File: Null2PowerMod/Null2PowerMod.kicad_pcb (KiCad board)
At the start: 2 copper layers, 18 x 28 mm, 35 parts, among them CN4 USB_C_Receptacle_USB2.0, J1 Conn_01x01, J2 Conn_01x08, J3 Conn_01x01, J4 Conn_01x01, J5 Conn_01x01, T1 MMUN2133LT1G, U1 TPS61030PWP, U2 MCP73871

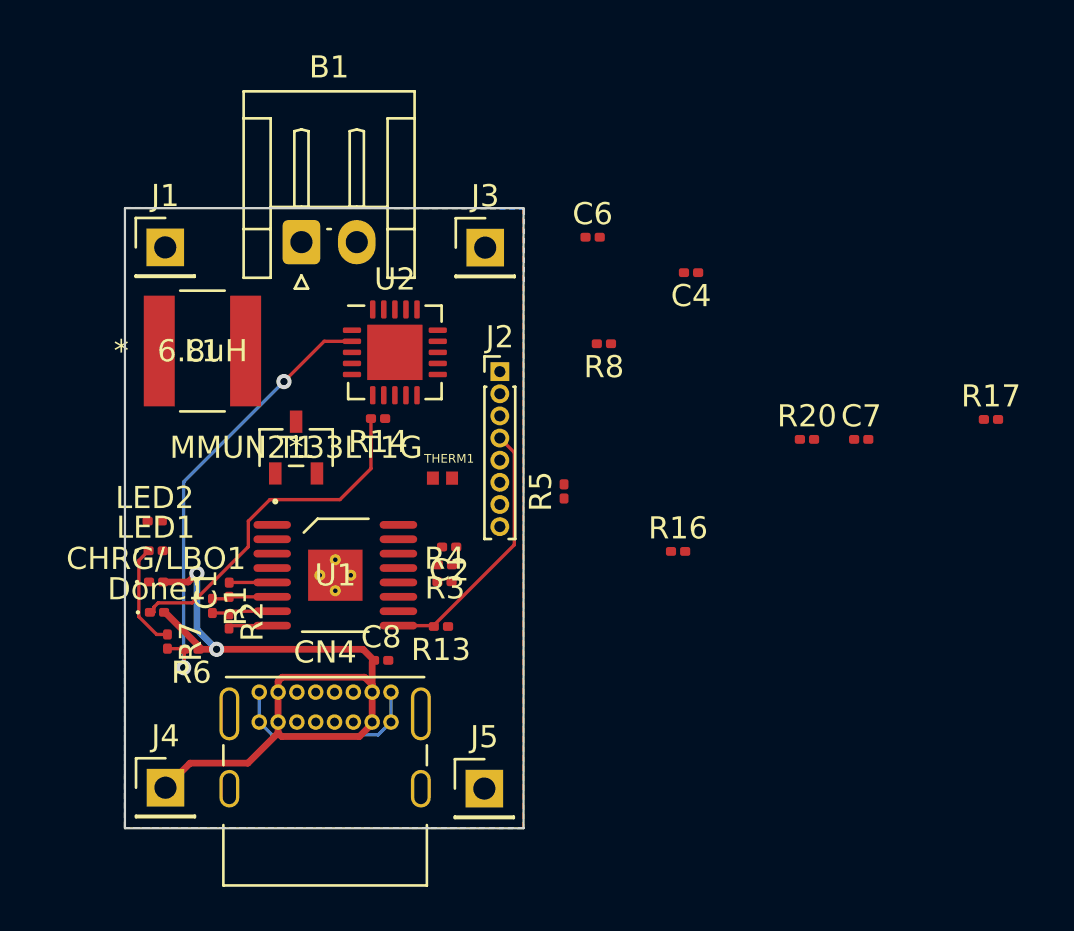
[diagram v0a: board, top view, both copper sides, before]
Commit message: Trying out an autorouter
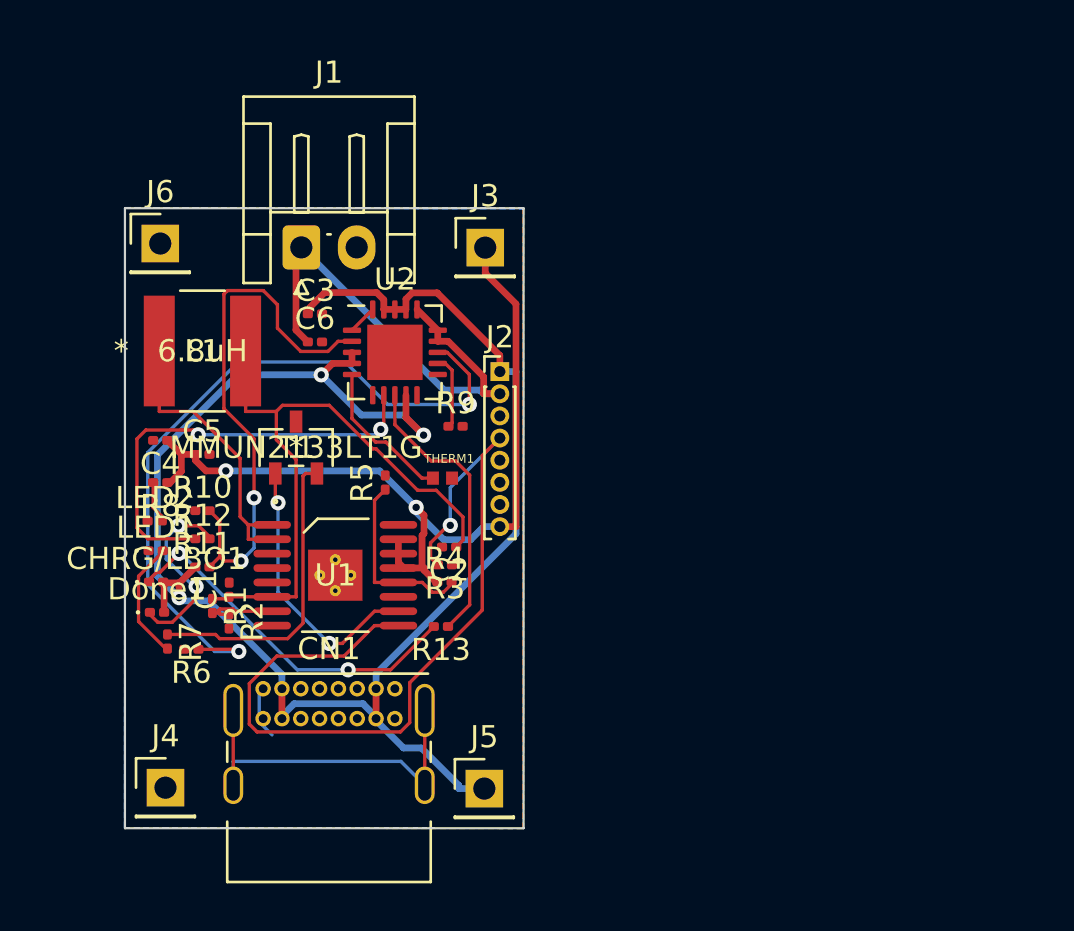
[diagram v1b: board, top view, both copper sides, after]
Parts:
- removed B1: Conn_01x02_Female, Connector_JST:JST_EH_S2B-EH_1x02_P2.50mm_Horizontal
- removed C7, C8: 10μF, Capacitor_SMD:C_0201_0603Metric
- removed CN4: USB_C_Receptacle_USB2.0, Connector_USB:USB_C_Receptacle_GCT_USB4085
- removed R14, R16, R20: 1k, Resistor_SMD:R_0201_0603Metric
- removed R17: 100k, Resistor_SMD:R_0201_0603Metric
- added C3: 10μF, Capacitor_SMD:C_0201_0603Metric, F.Cu at (68.6, 64.8)
- added C5: 100μF, Capacitor_SMD:C_0201_0603Metric, F.Cu at (63.5, 71.1)
- added CN1: USB_C_Receptacle_USB2.0, Connector_USB:USB_C_Receptacle_GCT_USB4085, F.Cu at (66.2, 81.7)
- added J6: Conn_01x01, Connector_PinHeader_2.54mm:PinHeader_1x01_P2.54mm_Vertical, F.Cu at (61.6, 61.6)
- added R10: 100k, Resistor_SMD:R_0201_0603Metric, F.Cu at (63.5, 73.7)
- added R11: 270k, Resistor_SMD:R_0201_0603Metric, F.Cu at (63.5, 76.2)
- added R12: 1k, Resistor_SMD:R_0201_0603Metric, F.Cu at (63.5, 74.9)
- added R9: 100k, Resistor_SMD:R_0201_0603Metric, F.Cu at (74.9, 69.8)
- C2: value 2.2μF -> 0.1μF
- C4: value 0.1μF -> 2.2μF
- C6: value 100μF -> 10μF
- J1: value Conn_01x01 -> Conn_01x02; footprint Connector_PinHeader_2.54mm:PinHeader_1x01_P2.54mm_Vertical -> Connector_JST:JST_EH_S2B-EH_1x02_P2.50mm_Horizontal
- R13: value 200k -> 1k
- R3: value 1.87M -> 200k
- R4: value 200k -> 1.87M
- R5: value 1k -> 200k; footprint Capacitor_SMD:C_0201_0603Metric -> Resistor_SMD:R_0201_0603Metric
- R6: value 270k -> 1k
- R7: value 100k -> 1k
- R8: footprint Resistor_SMD:R_0201_0603Metric -> Capacitor_SMD:C_0201_0603Metric
- moved C4 25.1 mm to (61.6, 70.5)
- moved R8 21.0 mm to (61.6, 72.4)
- moved C6 13.4 mm to (68.6, 66.0)
- moved R5 8.08 mm to (71.8, 72.4)
- moved J1 6.15 mm to (68.0, 61.8)
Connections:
- C2 pad 1: +5V -> Net-(C1-Pad1)
- C4 pad 1: Net-(C1-Pad1) -> +5V
- C6 pad 1: +5V -> VLIPO
- J1 pad 1: +5V -> VLIPO
- J3 pad 1: GND -> +5V
- J4 pad 1: VBUS -> GND
- J5 pad 1: GND -> VBUS
- R13 pad 2: /Enable -> Net-(CHRG/LBO1-Pad1)
- R3 pad 1: +5V -> Net-(R3-Pad1)
- R3 pad 2: Net-(R3-Pad2) -> /Enable
- R4 pad 1: Net-(R3-Pad2) -> +5V
- R4 pad 2: GND -> Net-(R4-Pad2)
- R5 pad 1: +5V -> Net-(R4-Pad2)
- R5 pad 2: Net-(LED2-Pad2) -> GND
- R6 pad 1: VBUS -> Net-(R6-Pad1)
- R6 pad 2: Net-(R6-Pad2) -> GND
- R7 pad 1: GND -> Net-(R7-Pad1)
- R7 pad 2: Net-(R6-Pad2) -> Net-(LED1-Pad2)
- R8 pad 1: Net-(R8-Pad1) -> +5V
- R8 pad 2: Net-(CHRG/LBO1-Pad1) -> Net-(LED2-Pad2)
- T1 pad 2: Net-(R20-Pad1) -> Net-(R7-Pad1)
- U1 pad 12: Net-(R3-Pad2) -> Net-(R4-Pad2)
- U2 pad 13: Net-(R16-Pad1) -> Net-(R6-Pad1)
- U2 pad 2: Net-(R6-Pad2) -> Net-(R10-Pad2)
- U2 pad 8: Net-(R8-Pad1) -> Net-(R13-Pad1)
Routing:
- net VBUS: track 36.7 -> 80.1 mm, vias 2 -> 3
- net +5V: track 0.00 -> 39.3 mm, vias 0 -> 2
- net Net-(R6-Pad1): track 0.00 -> 33.4 mm, vias 0 -> 2
- net /Enable: track 11.9 -> 39.0 mm, vias 0 -> 1
- net Net-(C1-Pad1): track 2.74 -> 28.8 mm
- net Net-(R10-Pad2): track 0.00 -> 24.6 mm, vias 0 -> 2
- net VLIPO: track 0.00 -> 22.4 mm
- net Net-(R6-Pad2): track 20.2 -> 0.00 mm, vias 2 -> 0
- net Net-(R12-Pad1): track 0.00 -> 19.8 mm, vias 0 -> 2
- net unconnected-(CN1-PadS1): track 0.00 -> 16.9 mm
- net Net-(CHRG/LBO1-Pad1): track 0.00 -> 16.4 mm, vias 0 -> 2
- net GND: track 17.9 -> 2.18 mm
- net Net-(R7-Pad1): track 0.00 -> 13.8 mm
- net SW: track 0.00 -> 13.2 mm
- net Net-(R13-Pad1): track 0.00 -> 12.9 mm
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
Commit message: Reset and try again
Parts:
- moved R8 106.4 mm to (163.7, 102.4), turned to 0 degrees
- moved C4 105.5 mm to (161.5, 104.5), turned to 0 degrees
- moved C5 102.7 mm to (161.2, 102.8)
- moved C6 101.2 mm to (161.5, 106.3)
- moved R1 100.4 mm to (161.7, 100.6), turned to 0 degrees
- moved R12 100.0 mm to (159.0, 104.5)
- moved R10 99.6 mm to (158.8, 102.8)
- moved C3 98.4 mm to (156.6, 108.8)
- moved R7 98.1 mm to (156.6, 105.3), turned to 0 degrees
- moved R11 95.2 mm to (154.1, 105.3)
- moved R9 94.4 mm to (164.2, 100.6)
- moved R5 93.6 mm to (159.0, 106.3), turned to 0 degrees
- moved R2 91.1 mm to (145.6, 120.6), turned to 0 degrees
- moved THERM1 89.4 mm to (159.0, 100.8)
- moved LED2 89.0 mm to (135.9, 122.8)
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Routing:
- net VBUS: track 80.1 -> 0.00 mm, vias 3 -> 0
- net +5V: track 39.3 -> 0.00 mm, vias 2 -> 0
- net /Enable: track 39.0 -> 0.00 mm, vias 1 -> 0
- net Net-(R6-Pad1): track 33.4 -> 0.00 mm, vias 2 -> 0
- net Net-(C1-Pad1): track 28.8 -> 0.00 mm
- net Net-(R10-Pad2): track 24.6 -> 0.00 mm, vias 2 -> 0
- net VLIPO: track 22.4 -> 0.00 mm
- net Net-(R12-Pad1): track 19.8 -> 0.00 mm, vias 2 -> 0
- net unconnected-(CN1-PadS1): track 16.9 -> 0.00 mm
- net Net-(CHRG/LBO1-Pad1): track 16.4 -> 0.00 mm, vias 2 -> 0
- net Net-(R7-Pad1): track 13.8 -> 0.00 mm
- net SW: track 13.2 -> 0.00 mm
- net Net-(R13-Pad1): track 12.9 -> 0.00 mm
- net Net-(T1-Pad1): track 12.4 -> 0.00 mm, vias 2 -> 0
- net Net-(Done1-Pad1): track 8.61 -> 0.00 mm, vias 2 -> 0
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- removed copper zone on B.Cu, net GND
- removed copper zone on F.Cu, net GND
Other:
- board size 18 x 28 mm -> 17.2 x 28 mm
